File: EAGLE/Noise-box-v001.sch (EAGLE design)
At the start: 41 parts, among them J1 AVR_SPI_PROG_3X22X3_LOCK, J2 BATT, J4 MICRO-SD_CARD_SOCKET, J5 AUDIO_JACK_3.5MM_SMD, U1 ATMEGA328P_TQFP, U2 MIC5219 3.3V, U3 MCP73831, Y1 12.288MHz

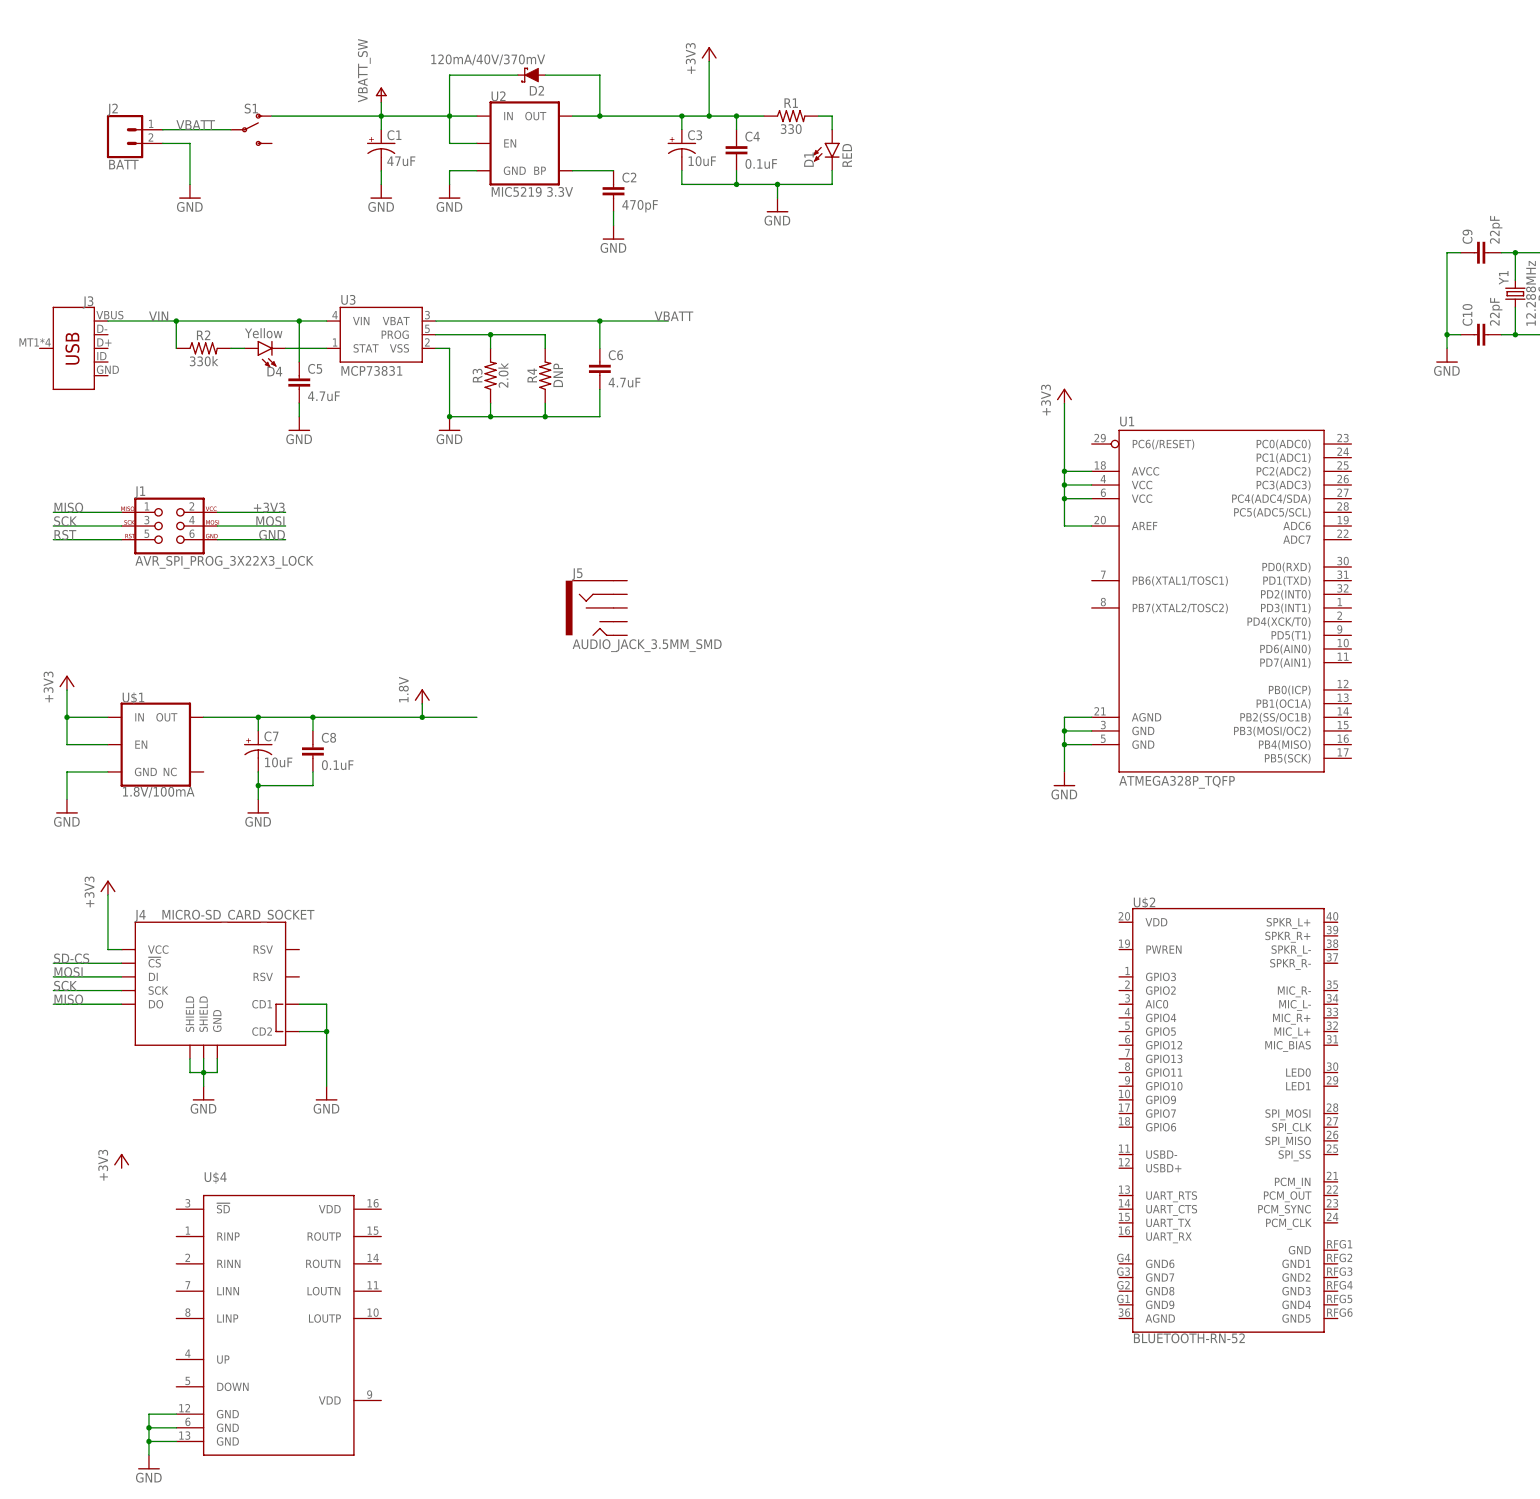
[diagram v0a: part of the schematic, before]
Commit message: Battery
Picked battery with best available Wh/dollar
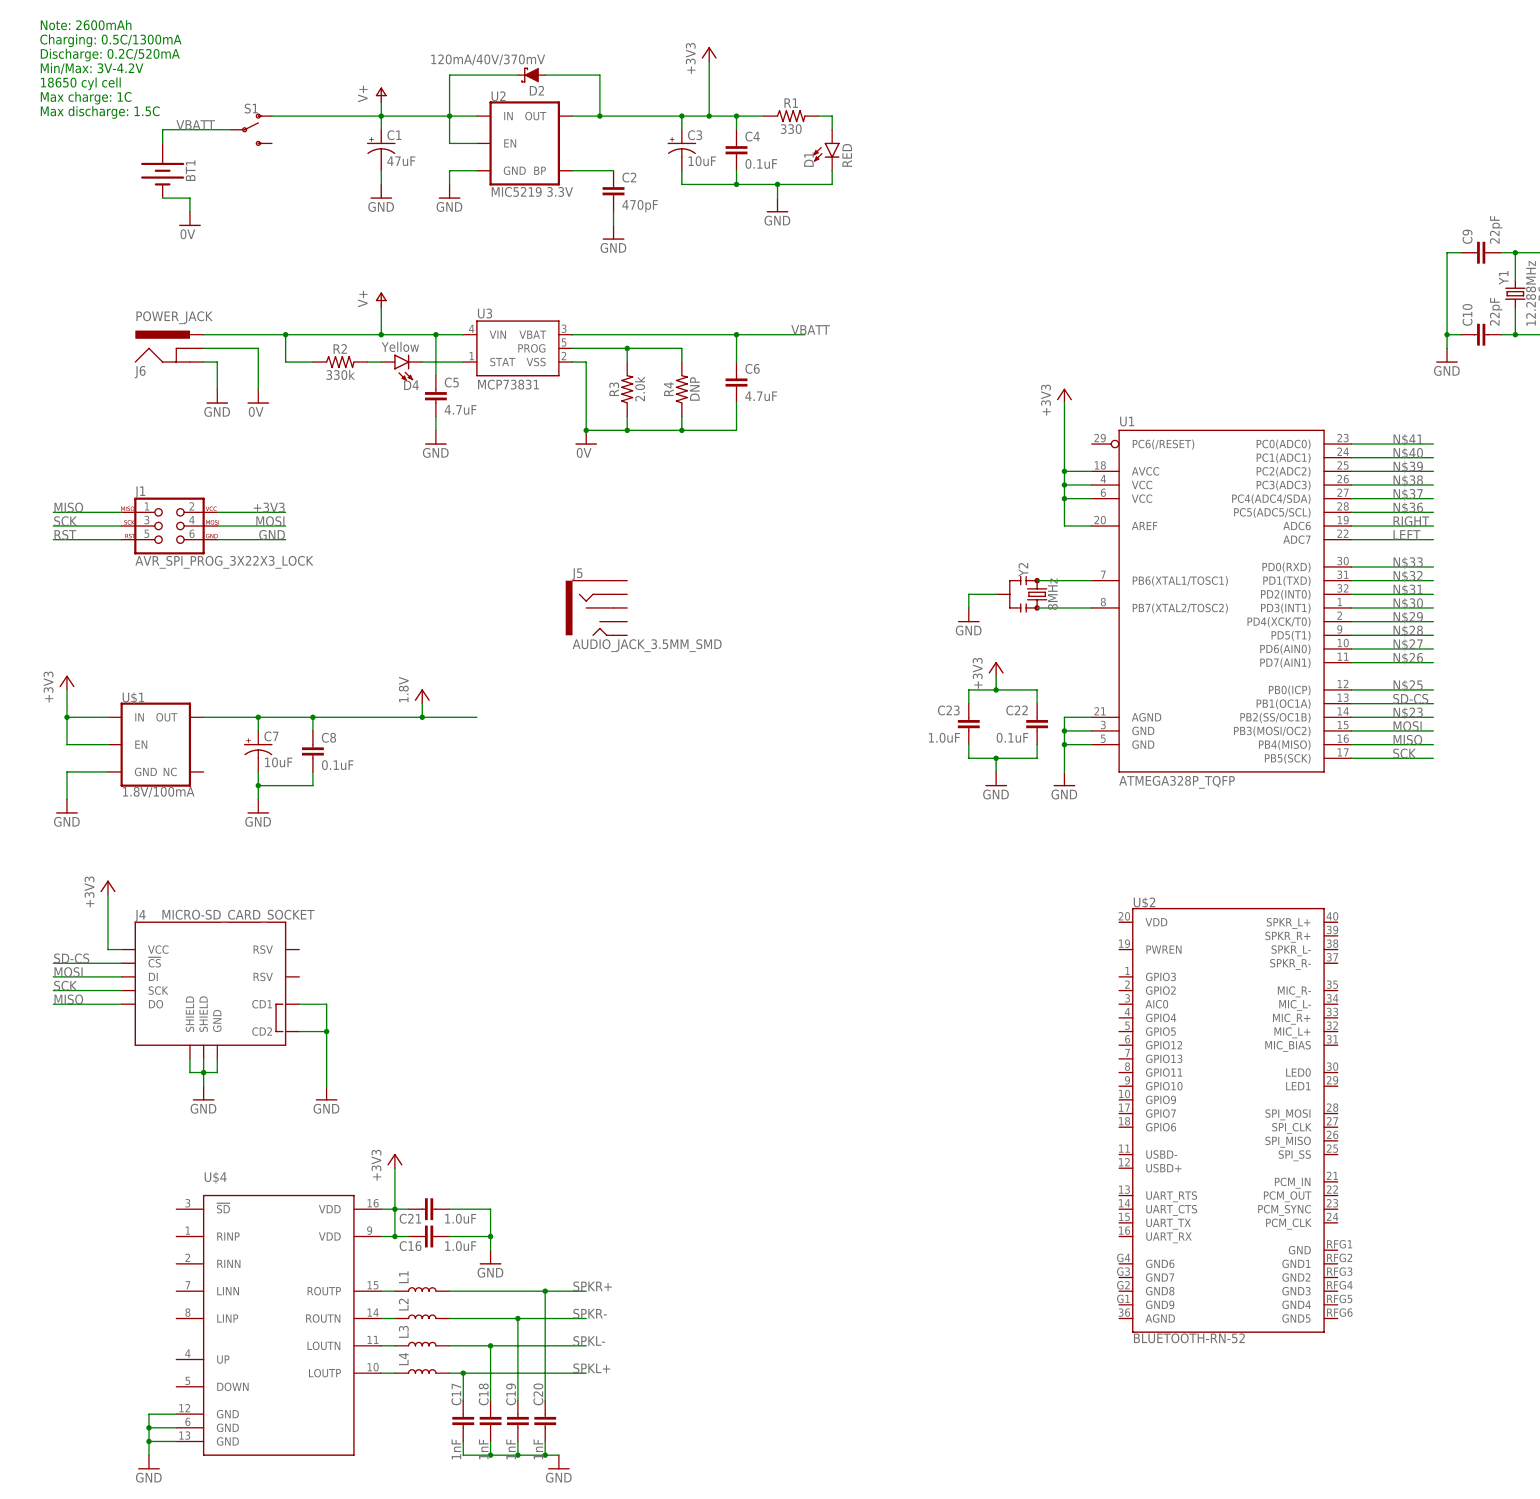
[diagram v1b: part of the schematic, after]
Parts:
- removed J2: BATT, SparkFun-Connectors:CONN_02-JST-2MM-SMT
- removed J3: (no value), SparkFun-Connectors:USB_MICRO-B_SMT
- added BT1: (no value), SparkFun-Batteries:BATTERY-18650
- added C16, C21, C23: 1.0uF, SparkFun-Capacitors:1.0UF-0603-16V-10%
- added C17, C18, C19, C20: 1nF, SparkFun-Capacitors:1.0NF/1000PF-0603-50V-10%
- added C22: 0.1uF, SparkFun-Capacitors:0.1UF-0603-25V-5%
- added J6: POWER_JACK, SparkFun-Connectors:POWER_JACK
- added L1, L2, L3, L4: INDUCTOR-0805-3.3UH, SparkFun-Coils:INDUCTOR-0805-3.3UH
- added Y2: 8MHz, SparkFun-Clocks:RESONATOR-8MHZSMD_3.2X1.3
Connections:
- removed net VIN: C5.1, J3.VBUS, R2.1, U3.VIN
- new net 0V: BT1.-, C6.2, J6.GNDBREAK, R3.1, R4.1, U3.VSS
- new net N$10: L2.1, U$4.ROUTN
- new net N$11: L3.1, U$4.LOUTN
- new net N$12: L4.1, U$4.LOUTP
- new net N$23: U1.PB2(SS/OC1B)
- new net N$25: U1.PB0(ICP)
- new net N$26: U1.PD7(AIN1)
- new net N$27: U1.PD6(AIN0)
- new net N$28: U1.PD5(T1)
- new net N$29: U1.PD4(XCK/T0)
- new net N$30: U1.PD3(INT1)
- new net N$31: U1.PD2(INT0)
- new net N$32: U1.PD1(TXD)
- new net N$33: U1.PD0(RXD)
- new net N$36: U1.PC5(ADC5/SCL)
- new net N$37: U1.PC4(ADC4/SDA)
- new net N$38: U1.PC3(ADC3)
- new net N$39: U1.PC2(ADC2)
- new net N$40: U1.PC1(ADC1)
- new net N$41: U1.PC0(ADC0)
- new net N$5: U1.PB6(XTAL1/TOSC1), Y2.1
- new net N$8: U1.PB7(XTAL2/TOSC2), Y2.3
- new net N$9: L1.1, U$4.ROUTP
- new net SPKL+: C17.1, L4.2
- new net SPKL-: C18.1, L3.2
- new net SPKR+: C20.1, L1.2
- new net SPKR-: C19.1, L2.2
- net +3V3: now also C16.1, C21.1, C22.1, C23.1, U$4.VDD@1, U$4.VDD@2
- net GND: now also C16.2, C17.2, C18.2, C19.2, C20.2, C21.2, C22.2, C23.2, J6.GND, Y2.2; no longer C6.2, J2.1, R3.1, R4.1, U3.VSS
- net LEFT: now also U1.ADC7
- net MISO: now also U1.PB4(MISO)
- net MOSI: now also U1.PB3(MOSI/OC2)
- net RIGHT: now also U1.ADC6
- net SCK: now also U1.PB5(SCK)
- net SD-CS: now also U1.PB1(OC1A)
- net V+: now also C5.1, J6.PWR, R2.1, U3.VIN
- net VBATT: now also BT1.+; no longer J2.2
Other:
- note added: "Note: 2600mAh Charging: 0.5C/1300mA Discharge: 0.2C/520mA Min/Max: 3V-4.2V 18650 cyl cell Max charge: 1C Max discharge: 1.5C"
- moved on the sheet: C5, C6, D4, R2, R3, R4, U3

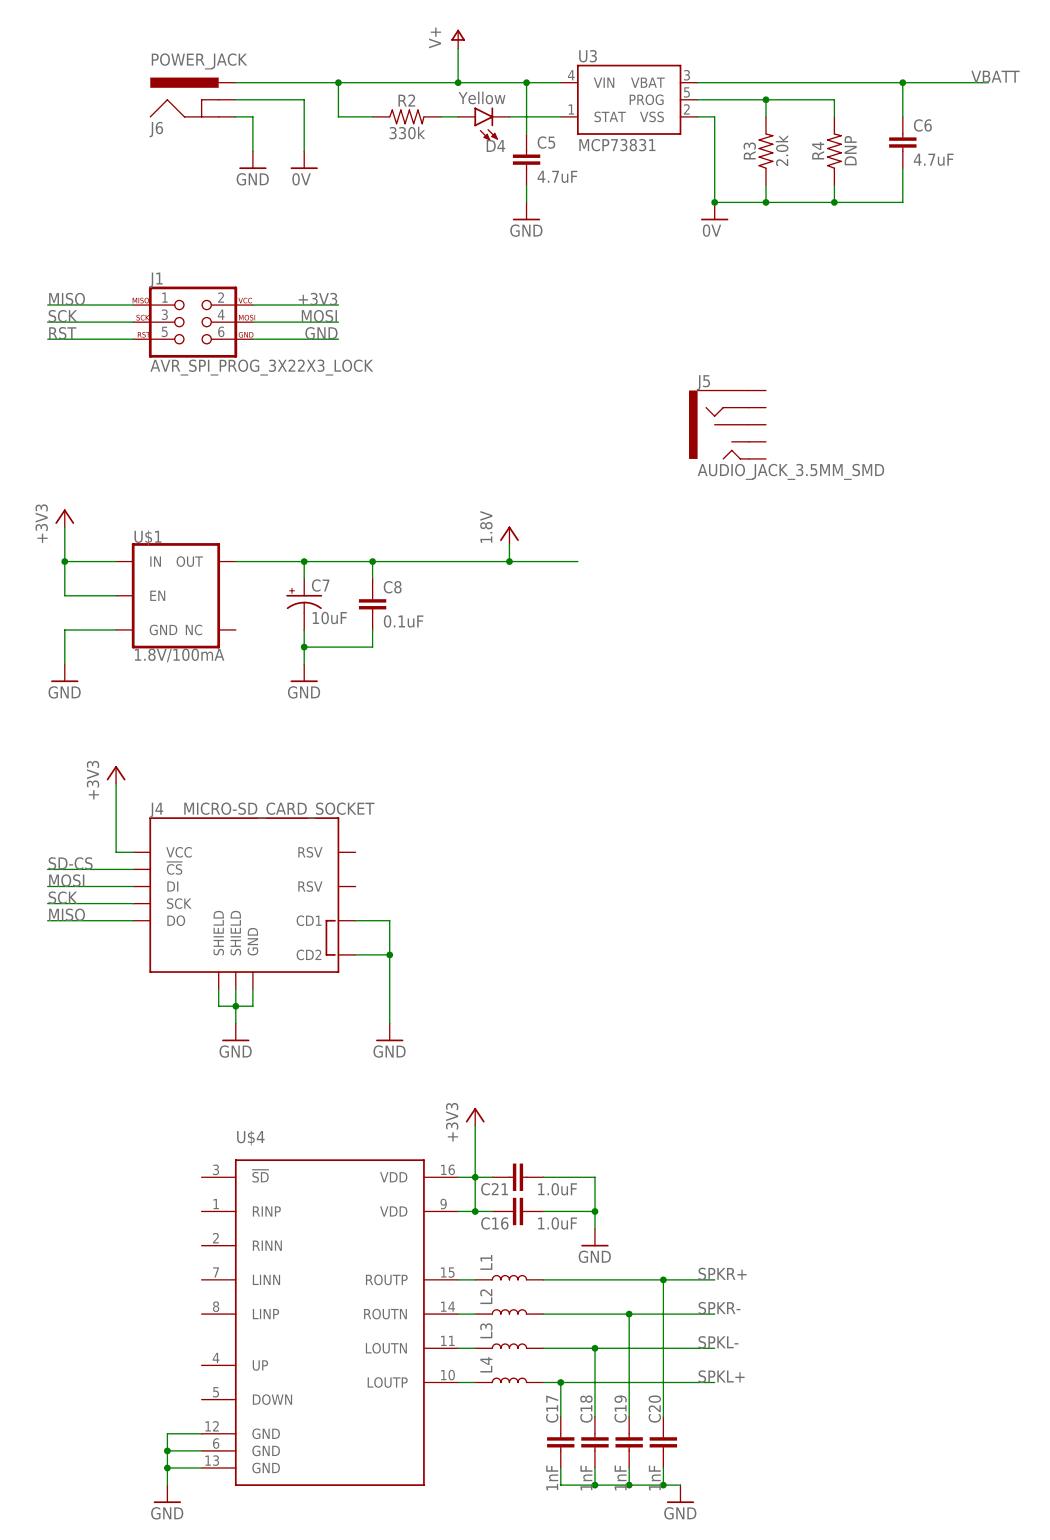
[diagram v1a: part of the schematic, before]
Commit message: Layout
First pass at layout. Established rough board dimensions. It seems that
establishing GND different than Battery (-) will necessitate a long
trace through the middle of the board. This might be avoided by going
with a wire lead version of the battery holder and avoiding that
unwanted trace by use of wires.
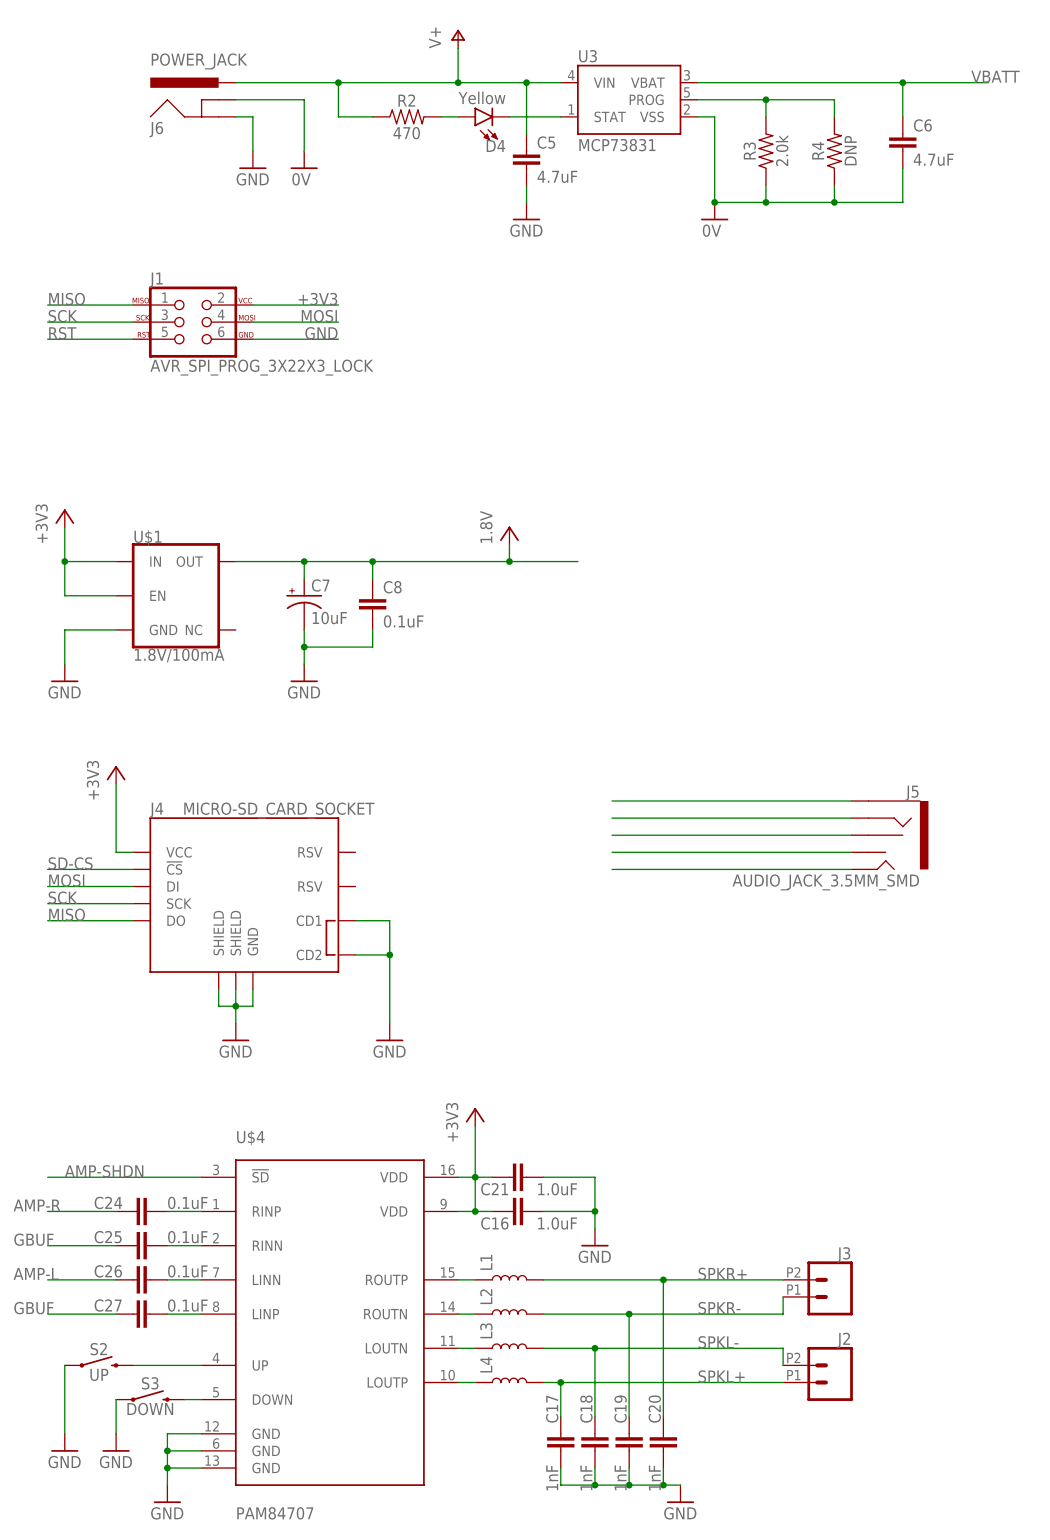
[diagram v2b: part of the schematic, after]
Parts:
- added C24, C25, C26, C27: 0.1uF, SparkFun-Capacitors:0.1UF-0603-25V-5%
- added J2, J3: (no value), SparkFun-Connectors:CONN_022.54MM_SCREWTERM
- added S2: UP, SparkFun-Switches:MOMENTARY-SWITCH-SPST-PTH-6.0MM
- added S3: DOWN, SparkFun-Switches:MOMENTARY-SWITCH-SPST-PTH-6.0MM
- R2: value 330k -> 470; device SparkFun-Resistors:330KOHM-0603-1/10W-1% -> SparkFun-Resistors:470OHM-0603-1/10W-1%
- U$4: value (none) -> PAM84707
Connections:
- new net AMP-L: C26.1
- new net AMP-R: C24.1
- new net AMP-SHDN: U$4.!SD
- new net N$13: J5.SLEEVE
- new net N$16: J5.RING
- new net N$19: J5.RSH
- new net N$20: J5.TSH
- new net N$22: J5.TIP
- new net N$24: C24.2, U$4.RINP
- new net N$34: C25.2, U$4.RINN
- new net N$35: C26.2, U$4.LINN
- new net N$42: C27.2, U$4.LINP
- new net N$43: S3.2, U$4.DOWN
- new net N$44: S2.2, U$4.UP
- net GBUF: now also C25.1, C27.1
- net GND: now also S2.1, S3.1
- net SPKL+: now also J2.1
- net SPKL-: now also J2.2
- net SPKR+: now also J3.2
- net SPKR-: now also J3.1
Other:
- moved on the sheet: J5

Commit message: Layout updates
Adjusted battery holder package. Began layout, establishing rough
dimensions of the board.
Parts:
- removed BT1: (no value), SparkFun-Batteries:BATTERY-18650
- added BT2: (no value), MAK:BATTERY-1043P
- added R10, R11, R12: 100k, SparkFun-Resistors:100KOHM-0603-1/10W-1%
- R7: value RN-4_100K -> 100k; device RJC-2:RN-4_100K -> SparkFun-Resistors:100KOHM-0603-1/10W-1%
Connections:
- removed net 0V: BT1.-, C6.2, J6.GNDBREAK, R3.1, R4.1, U3.VSS
- removed net V+: C1.+, C5.1, D2.C, J6.PWR, R2.1, S1.O, U2.EN, U2.IN, U3.VIN
- new net N$45: C1.+, D2.C, S1.O, U2.EN, U2.IN
- new net VIN: C5.1, J6.PWR, R2.1, U3.VIN
- net EN-GPIO1: now also R11.2; no longer R7-3.2
- net GND: now also BT2.-, C6.2, J6.GNDBREAK, R10.1, R11.1, R12.1, R3.1, R4.1, R7.1, U3.VSS; no longer R7-1.1, R7-2.1, R7-3.1, R7-4.1
- net GPIO0: now also R12.2; no longer R7-4.2
- net N$14: now also R7.2; no longer R7-1.2
- net N$15: now also R10.2; no longer R7-2.2
- net VBATT: now also BT2.+; no longer BT1.+

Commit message: Layout
continued layout design. updated a few minor schematic errors
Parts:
- added C28, C29: 10nF, SparkFun-Capacitors:10NF-0603-50V-10%
- added C30: 47nF, SparkFun-Capacitors:47NF-0603-25V-5%
- added JP1: SJ1, SparkFun-Jumpers:JUMPER-SMT_2_NO_SILK
- added JP2: SJ2, SparkFun-Jumpers:JUMPER-SMT_2_NO_SILK
- added R13, R14, R15, R16, R17: 10, SparkFun-Resistors:10OHM-0603-1/10W-5%
- added R18: 10k, SparkFun-Resistors:10KOHM-0603-1/10W-1%
- J5: value AUDIO_JACK_3.5MM_SMD -> HEADPHONE
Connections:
- removed net EN-GPIO1: R11.2, U$3.GPIO1/I2S_SDATA
- removed net N$25: U1.PB0(ICP)
- removed net N$26: U1.PD7(AIN1)
- removed net N$27: U1.PD6(AIN0)
- removed net N$31: U1.PD2(INT0)
- removed net N$39: U1.PC2(ADC2)
- net +3V3: now also R18.2
- net AMP-L: now also J5.TSH, JP1.2
- net AMP-R: now also J5.RSH, JP2.2
- net AMP-SHDN: now also R11.2, U$3.GPIO1/I2S_SDATA, U1.PC2(ADC2)
- net GBUF: now also J5.SLEEVE, R13.2
- net GND: now also C28.2, C29.2, C30.2
- net LEFT: now also J5.TIP, JP1.1, R16.2
- net MP3-CS: now also U1.PD6(AIN0)
- net MP3-DCS: now also U1.PD7(AIN1)
- net MP3-DREQ: now also U1.PD2(INT0)
- net MP3-RST: now also U1.PB0(ICP)
- net N$13: now also C28.1, R15.1; no longer J5.SLEEVE
- net N$16: now also C29.1, R14.1; no longer J5.RING
- net N$19: now also C30.1, R13.1; no longer J5.RSH
- net N$20: now also R15.2, R16.1; no longer J5.TSH
- net N$22: now also R14.2, R17.1; no longer J5.TIP
- net RIGHT: now also J5.RING, JP2.1, R17.2
- net RST: now also R18.1, U1.PC6(/RESET)
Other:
- moved on the sheet: J5
